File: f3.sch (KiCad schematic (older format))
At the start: 13 parts, among them U7 STM32F303K8Tx, Y1 Crystal

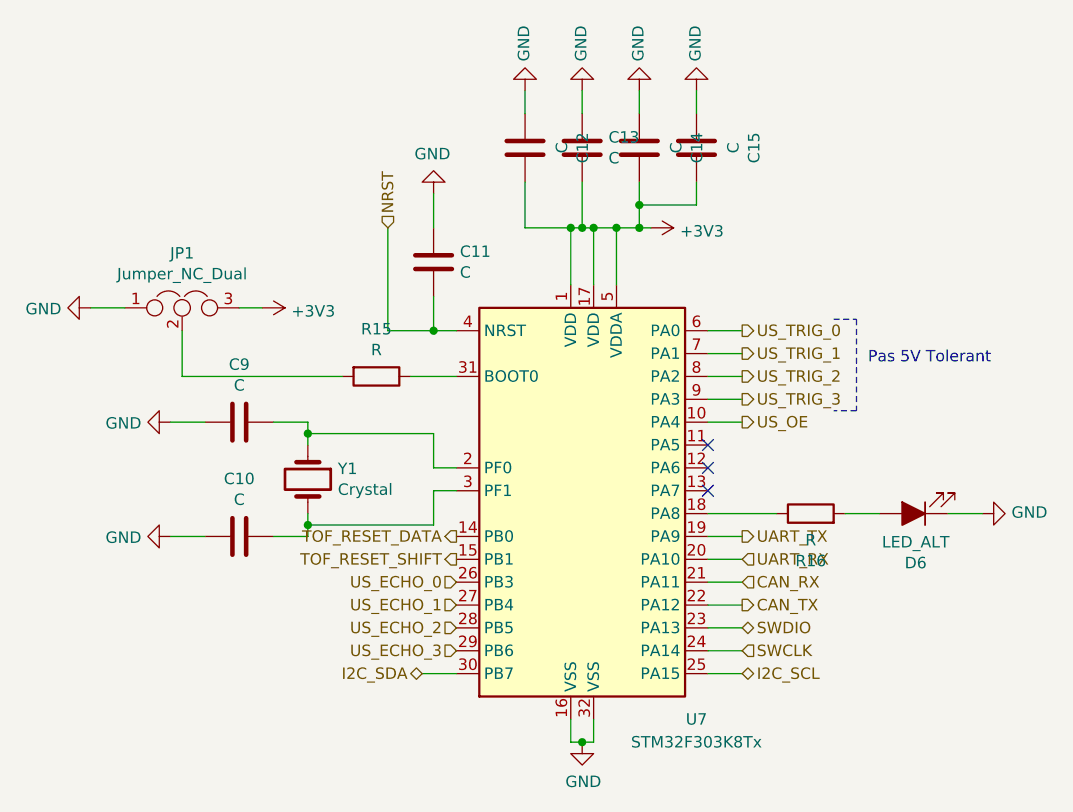
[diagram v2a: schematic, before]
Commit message: Schematic corrections
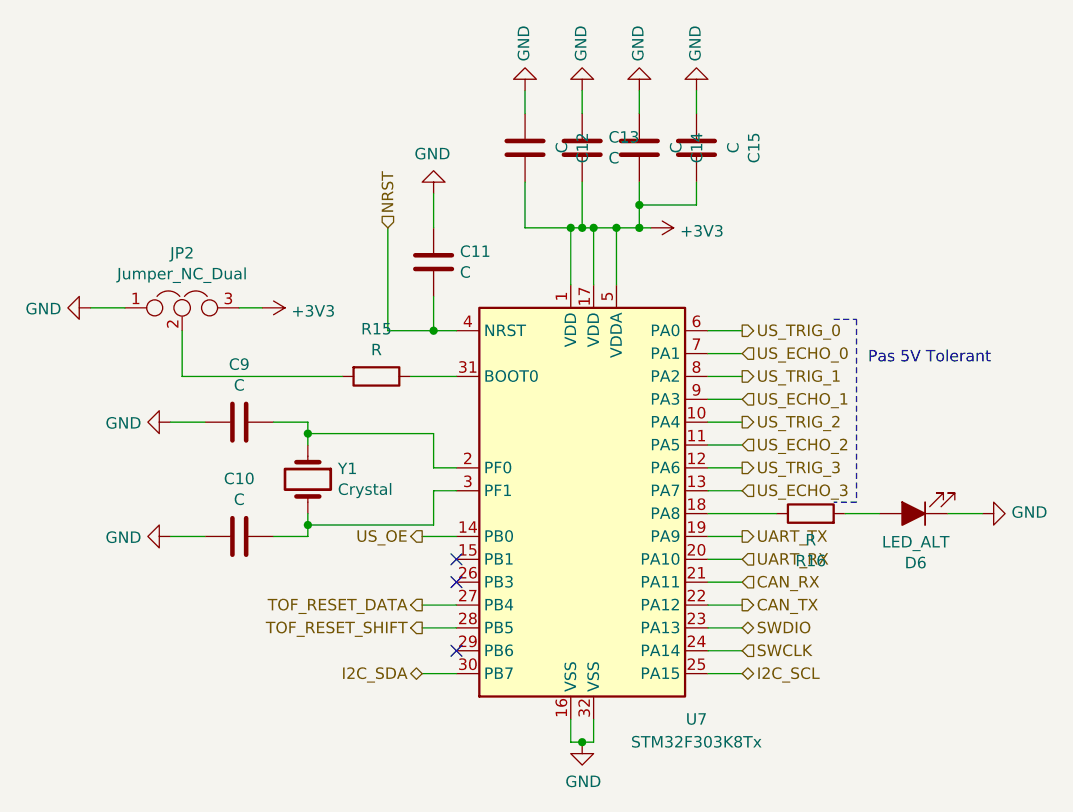
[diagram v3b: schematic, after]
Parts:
- renumbered JP1 to JP2
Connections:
- net TOF_RESET_DATA: now also U7.27 (PB4); no longer U7.14 (PB0)
- net TOF_RESET_SHIFT: now also U7.28 (PB5); no longer U7.15 (PB1)
- net US_ECHO_0: now also U7.7 (PA1); no longer U7.26 (PB3)
- net US_ECHO_1: now also U7.9 (PA3); no longer U7.27 (PB4)
- net US_ECHO_2: now also U7.11 (PA5); no longer U7.28 (PB5)
- net US_ECHO_3: now also U7.13 (PA7); no longer U7.29 (PB6)
- net US_OE: now also U7.14 (PB0); no longer U7.10 (PA4)
- net US_TRIG_1: now also U7.8 (PA2); no longer U7.7 (PA1)
- net US_TRIG_2: now also U7.10 (PA4); no longer U7.8 (PA2)
- net US_TRIG_3: now also U7.12 (PA6); no longer U7.9 (PA3)
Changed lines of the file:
@@
 $EndComp
 $Comp
-L power:GND #PWR059
+L power:GND #PWR058
 U 1 1 5BBD4293
 P 3500 3500
-F 0 "#PWR059" H 3500 3250 50  0001 C CNN
+F 0 "#PWR058" H 3500 3250 50  0001 C CNN
 F 1 "GND" V 3505 3372 50  0000 R CNN
 F 2 "" H 3500 3500 50  0001 C CNN
@@
 $EndComp
 $Comp
-L power:GND #PWR060
+L power:GND #PWR059
 U 1 1 5BBD42C5
 P 3500 4000
-F 0 "#PWR060" H 3500 3750 50  0001 C CNN
+F 0 "#PWR059" H 3500 3750 50  0001 C CNN
 F 1 "GND" V 3505 3872 50  0000 R CNN
 F 2 "" H 3500 4000 50  0001 C CNN
@@
 $EndComp
 $Comp
-L Device:Jumper_NC_Dual JP1
+L Device:Jumper_NC_Dual JP2
 U 1 1 5BBD452E
 P 3550 3000
-F 0 "JP1" H 3550 3239 50  0000 C CNN
+F 0 "JP2" H 3550 3239 50  0000 C CNN
 F 1 "Jumper_NC_Dual" H 3550 3148 50  0000 C CNN
 F 2 "Connector_PinHeader_2.54mm:PinHeader_1x03_P2.54mm_Vertical" H 3550 3000 50  0001 C CNN
@@
 	4550 3300 4750 3300
 $Comp
-L power:GND #PWR058
+L power:GND #PWR057
 U 1 1 5BBD4A9A
 P 3150 3000
-F 0 "#PWR058" H 3150 2750 50  0001 C CNN
+F 0 "#PWR057" H 3150 2750 50  0001 C CNN
 F 1 "GND" V 3155 2872 50  0000 R CNN
 F 2 "" H 3150 3000 50  0001 C CNN
@@
 	3150 3000 3300 3000
 $Comp
-L power:+3V3 #PWR061
+L power:+3V3 #PWR060
 U 1 1 5BBD4C69
 P 3900 3000
-F 0 "#PWR061" H 3900 2850 50  0001 C CNN
+F 0 "#PWR060" H 3900 2850 50  0001 C CNN
 F 1 "+3V3" V 3915 3128 50  0000 L CNN
 F 2 "" H 3900 3000 50  0001 C CNN
@@
 $EndComp
 $Comp
-L power:GND #PWR062
+L power:GND #PWR061
 U 1 1 5BBD55CA
 P 4650 2500
-F 0 "#PWR062" H 4650 2250 50  0001 C CNN
+F 0 "#PWR061" H 4650 2250 50  0001 C CNN
 F 1 "GND" H 4655 2327 50  0000 C CNN
 F 2 "" H 4650 2500 50  0001 C CNN
@@
 	5350 2650 5450 2650
 $Comp
-L power:+3V3 #PWR067
+L power:+3V3 #PWR066
 U 1 1 5BBD6204
 P 5600 2650
-F 0 "#PWR067" H 5600 2500 50  0001 C CNN
+F 0 "#PWR066" H 5600 2500 50  0001 C CNN
 F 1 "+3V3" V 5615 2778 50  0000 L CNN
 F 2 "" H 5600 2650 50  0001 C CNN
@@
 $EndComp
 $Comp
-L power:GND #PWR068
+L power:GND #PWR067
 U 1 1 5BBD68AE
 P 5800 2050
-F 0 "#PWR068" H 5800 1800 50  0001 C CNN
+F 0 "#PWR067" H 5800 1800 50  0001 C CNN
 F 1 "GND" V 5805 1922 50  0000 R CNN
 F 2 "" H 5800 2050 50  0001 C CNN
@@
 $EndComp
 $Comp
-L power:GND #PWR066
+L power:GND #PWR065
 U 1 1 5BBD68FC
 P 5550 2050
-F 0 "#PWR066" H 5550 1800 50  0001 C CNN
+F 0 "#PWR065" H 5550 1800 50  0001 C CNN
 F 1 "GND" V 5555 1922 50  0000 R CNN
 F 2 "" H 5550 2050 50  0001 C CNN
@@
 $EndComp
 $Comp
-L power:GND #PWR064
+L power:GND #PWR063
 U 1 1 5BBD694A
 P 5300 2050
-F 0 "#PWR064" H 5300 1800 50  0001 C CNN
+F 0 "#PWR063" H 5300 1800 50  0001 C CNN
 F 1 "GND" V 5305 1922 50  0000 R CNN
 F 2 "" H 5300 2050 50  0001 C CNN
@@
 $EndComp
 $Comp
-L power:GND #PWR063
+L power:GND #PWR062
 U 1 1 5BBD6998
 P 5050 2050
-F 0 "#PWR063" H 5050 1800 50  0001 C CNN
+F 0 "#PWR062" H 5050 1800 50  0001 C CNN
 F 1 "GND" V 5055 1922 50  0000 R CNN
 F 2 "" H 5050 2050 50  0001 C CNN
@@
 	5550 2550 5550 2650
 $Comp
-L power:GND #PWR065
+L power:GND #PWR064
 U 1 1 5BBDA4B0
 P 5300 4900
-F 0 "#PWR065" H 5300 4650 50  0001 C CNN
+F 0 "#PWR064" H 5300 4650 50  0001 C CNN
 F 1 "GND" H 5305 4727 50  0000 C CNN
 F 2 "" H 5300 4900 50  0001 C CNN
@@
 $EndComp
 $Comp
-L power:GND #PWR069
+L power:GND #PWR068
 U 1 1 5BBDC410
 P 7050 3900
-F 0 "#PWR069" H 7050 3650 50  0001 C CNN
+F 0 "#PWR068" H 7050 3650 50  0001 C CNN
 F 1 "GND" V 7055 3772 50  0000 R CNN
 F 2 "" H 7050 3900 50  0001 C CNN
@@
 Text HLabel 6000 3100 2    50   Output ~ 0
 US_TRIG_0
-Text HLabel 6000 3200 2    50   Output ~ 0
+Text HLabel 6000 3300 2    50   Output ~ 0
 US_TRIG_1
-Text HLabel 6000 3300 2    50   Output ~ 0
+Text HLabel 6000 3500 2    50   Output ~ 0
 US_TRIG_2
-Text HLabel 6000 3400 2    50   Output ~ 0
+Text HLabel 6000 3700 2    50   Output ~ 0
 US_TRIG_3
-Text HLabel 4750 4200 0    50   Input ~ 0
+Text HLabel 6000 3200 2    50   Input ~ 0
 US_ECHO_0
-Text HLabel 4750 4300 0    50   Input ~ 0
+Text HLabel 6000 3400 2    50   Input ~ 0
 US_ECHO_1
-Text HLabel 4750 4400 0    50   Input ~ 0
+Text HLabel 6000 3600 2    50   Input ~ 0
 US_ECHO_2
-Text HLabel 4750 4500 0    50   Input ~ 0
-US_ECHO_3
-Text HLabel 4750 4000 0    50   Output ~ 0
+Text HLabel 4600 4300 0    50   Output ~ 0
 TOF_RESET_DATA
-Text HLabel 4750 4100 0    50   Output ~ 0
+Text HLabel 4600 4400 0    50   Output ~ 0
 TOF_RESET_SHIFT
-NoConn ~ 5850 3800
-NoConn ~ 5850 3700
-NoConn ~ 5850 3600
 Text Notes 6550 3250 0    50   ~ 0
 Pas 5V Tolerant
 Wire Notes Line
 	6400 3050 6500 3050
-Wire Notes Line
-	6500 3050 6500 3450
-Wire Notes Line
-	6500 3450 6400 3450
-Text HLabel 6000 3500 2    50   Output ~ 0
+Text HLabel 4600 4000 0    50   Output ~ 0
 US_OE
 Wire Wire Line
@@
 	0    1    1    0
 $EndComp
+Wire Wire Line
+	5850 3600 6000 3600
+Wire Wire Line
+	5850 3700 6000 3700
+Text HLabel 6000 3800 2    50   Input ~ 0
+US_ECHO_3
+Wire Notes Line
+	6500 3850 6400 3850
+Wire Notes Line
+	6500 3050 6500 3850
+Wire Wire Line
+	5850 3800 6000 3800
+Wire Wire Line
+	4600 4000 4750 4000
+Wire Wire Line
+	4600 4300 4750 4300
+Wire Wire Line
+	4600 4400 4750 4400
+NoConn ~ 4750 4200
+NoConn ~ 4750 4500
+NoConn ~ 4750 4100
 $EndSCHEMATC

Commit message: Corrected, routing redone
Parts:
- JP2: footprint Connector_PinHeader_2.54mm:PinHeader_1x03_P2.54mm_Vertical -> Jumper:SolderJumper-3_P1.3mm_Open_RoundedPad1.0x1.5mm
- Y1: footprint Crystal:Crystal_HC49-U_Vertical -> Crystal:Crystal_HC49-4H_Vertical
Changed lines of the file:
@@
 F 0 "JP2" H 3550 3239 50  0000 C CNN
 F 1 "Jumper_NC_Dual" H 3550 3148 50  0000 C CNN
-F 2 "Connector_PinHeader_2.54mm:PinHeader_1x03_P2.54mm_Vertical" H 3550 3000 50  0001 C CNN
+F 2 "Jumper:SolderJumper-3_P1.3mm_Open_RoundedPad1.0x1.5mm" H 3550 3000 50  0001 C CNN
 F 3 "~" H 3550 3000 50  0001 C CNN
 	1    3550 3000
@@
 F 0 "Y1" V 4054 3881 50  0000 L CNN
 F 1 "Crystal" V 4145 3881 50  0000 L CNN
-F 2 "Crystal:Crystal_HC49-U_Vertical" H 4100 3750 50  0001 C CNN
+F 2 "Crystal:Crystal_HC49-4H_Vertical" H 4100 3750 50  0001 C CNN
 F 3 "~" H 4100 3750 50  0001 C CNN
 	1    4100 3750

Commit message: Added RS refs
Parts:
- D6: RS (none) -> 174-9844,174-9849
- Y1: RS (none) -> 814-9440
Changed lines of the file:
@@
 F 2 "LED_SMD:LED_0805_2012Metric_Castellated" H 6750 3900 50  0001 C CNN
 F 3 "~" H 6750 3900 50  0001 C CNN
+F 4 "174-9844,174-9849" H 0   0   50  0001 C CNN "RS"
 	1    6750 3900
 	-1   0    0    1
@@
 F 2 "Crystal:Crystal_HC49-4H_Vertical" H 4100 3750 50  0001 C CNN
 F 3 "~" H 4100 3750 50  0001 C CNN
+F 4 "814-9440" H 0   0   50  0001 C CNN "RS"
 	1    4100 3750
 	0    1    1    0

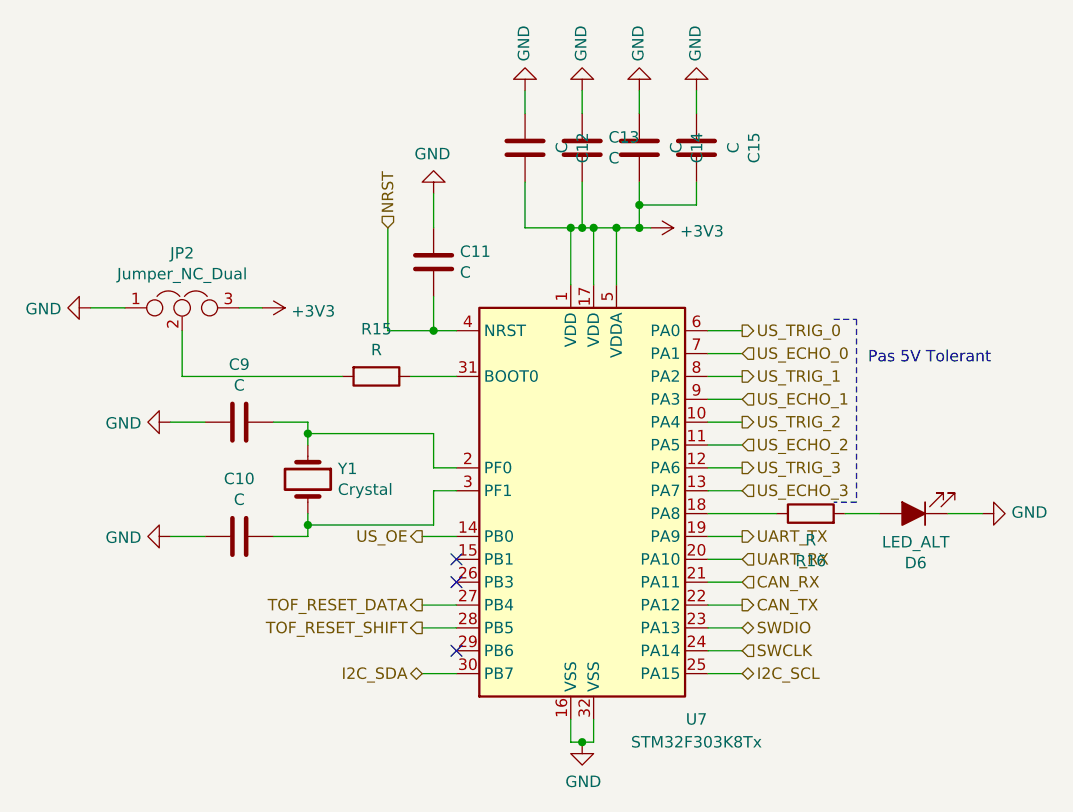
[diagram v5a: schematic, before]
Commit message: Added component values
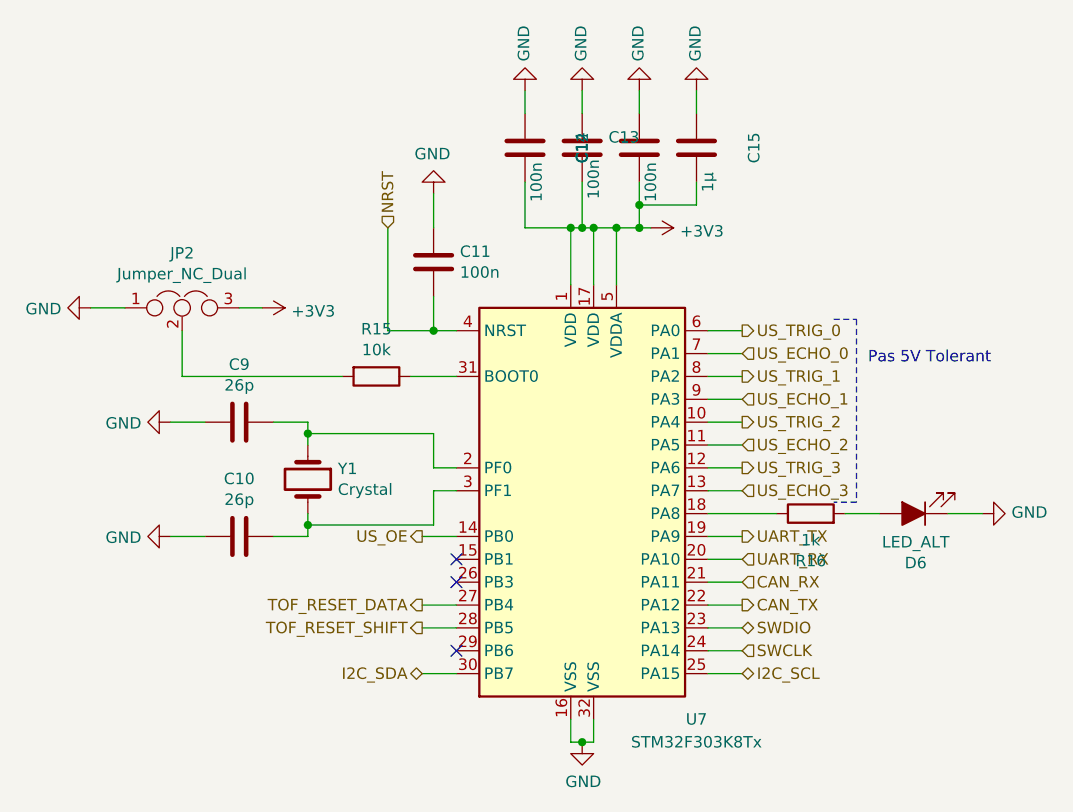
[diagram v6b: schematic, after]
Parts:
- C10, C9: value C -> 26p
- C11, C12, C13, C14: value C -> 100n
- C15: value C -> 1µ
- R15: value R -> 10k
- R16: value R -> 1k
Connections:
- net +3V3: now also C14.2; no longer C14.1
- net GND: now also C14.1; no longer C14.2
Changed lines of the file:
@@
 EESchema Schematic File Version 4
-LIBS:ultraphotonicsense-elec-cache
 EELAYER 26 0
 EELAYER END
@@
 P 3800 3500
 F 0 "C9" V 3548 3500 50  0000 C CNN
-F 1 "C" V 3639 3500 50  0000 C CNN
+F 1 "26p" V 3639 3500 50  0000 C CNN
 F 2 "Capacitor_SMD:C_0805_2012Metric_Pad1.15x1.40mm_HandSolder" H 3838 3350 50  0001 C CNN
 F 3 "~" H 3800 3500 50  0001 C CNN
@@
 P 3800 4000
 F 0 "C10" V 3548 4000 50  0000 C CNN
-F 1 "C" V 3639 4000 50  0000 C CNN
+F 1 "26p" V 3639 4000 50  0000 C CNN
 F 2 "Capacitor_SMD:C_0805_2012Metric_Pad1.15x1.40mm_HandSolder" H 3838 3850 50  0001 C CNN
 F 3 "~" H 3800 4000 50  0001 C CNN
@@
 P 4400 3300
 F 0 "R15" V 4193 3300 50  0000 C CNN
-F 1 "R" V 4284 3300 50  0000 C CNN
+F 1 "10k" V 4284 3300 50  0000 C CNN
 F 2 "Resistor_SMD:R_0805_2012Metric_Pad1.15x1.40mm_HandSolder" V 4330 3300 50  0001 C CNN
 F 3 "~" H 4400 3300 50  0001 C CNN
@@
 P 4650 2800
 F 0 "C11" H 4765 2846 50  0000 L CNN
-F 1 "C" H 4765 2755 50  0000 L CNN
+F 1 "100n" H 4765 2755 50  0000 L CNN
 F 2 "Capacitor_SMD:C_0805_2012Metric_Pad1.15x1.40mm_HandSolder" H 4688 2650 50  0001 C CNN
 F 3 "~" H 4650 2800 50  0001 C CNN
@@
 P 5050 2300
 F 0 "C12" V 4798 2300 50  0000 C CNN
-F 1 "C" V 4889 2300 50  0000 C CNN
+F 1 "100n" V 5000 2450 50  0000 C CNN
 F 2 "Capacitor_SMD:C_0805_2012Metric_Pad1.15x1.40mm_HandSolder" H 5088 2150 50  0001 C CNN
 F 3 "~" H 5050 2300 50  0001 C CNN
@@
 P 5300 2300
 F 0 "C13" H 5185 2346 50  0000 R CNN
-F 1 "C" H 5185 2255 50  0000 R CNN
+F 1 "100n" V 5250 2250 50  0000 R CNN
 F 2 "Capacitor_SMD:C_0805_2012Metric_Pad1.15x1.40mm_HandSolder" H 5338 2150 50  0001 C CNN
 F 3 "~" H 5300 2300 50  0001 C CNN
@@
 P 5550 2300
 F 0 "C14" V 5298 2300 50  0000 C CNN
-F 1 "C" V 5389 2300 50  0000 C CNN
+F 1 "100n" V 5600 2150 50  0000 C CNN
 F 2 "Capacitor_SMD:C_0805_2012Metric_Pad1.15x1.40mm_HandSolder" H 5588 2150 50  0001 C CNN
 F 3 "~" H 5550 2300 50  0001 C CNN
 	1    5550 2300
-	-1   0    0    1
+	1    0    0    -1
 $EndComp
 $Comp
@@
 P 5800 2300
 F 0 "C15" V 5548 2300 50  0000 C CNN
-F 1 "C" V 5639 2300 50  0000 C CNN
+F 1 "1µ" V 5750 2450 50  0000 C CNN
 F 2 "Capacitor_SMD:C_0805_2012Metric_Pad1.15x1.40mm_HandSolder" H 5838 2150 50  0001 C CNN
 F 3 "~" H 5800 2300 50  0001 C CNN
@@
 P 6300 3900
 F 0 "R16" V 6093 3900 50  0000 C CNN
-F 1 "R" V 6184 3900 50  0000 C CNN
+F 1 "1k" V 6184 3900 50  0000 C CNN
 F 2 "Resistor_SMD:R_0805_2012Metric_Pad1.15x1.40mm_HandSolder" V 6230 3900 50  0001 C CNN
 F 3 "~" H 6300 3900 50  0001 C CNN

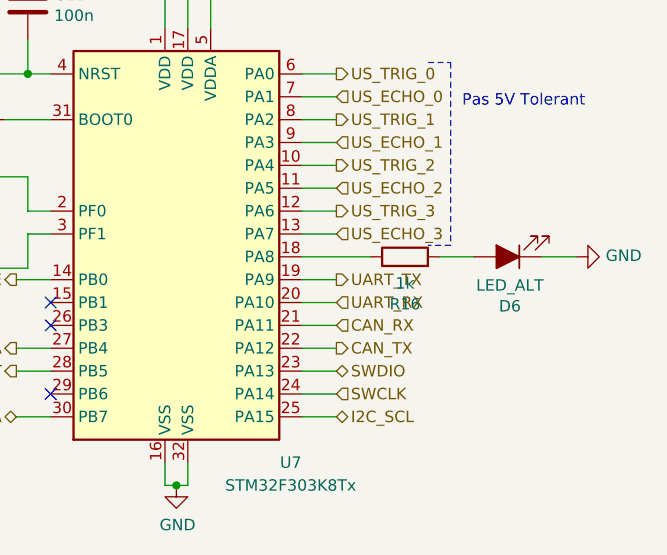
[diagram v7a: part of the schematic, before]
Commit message: Added resistors values
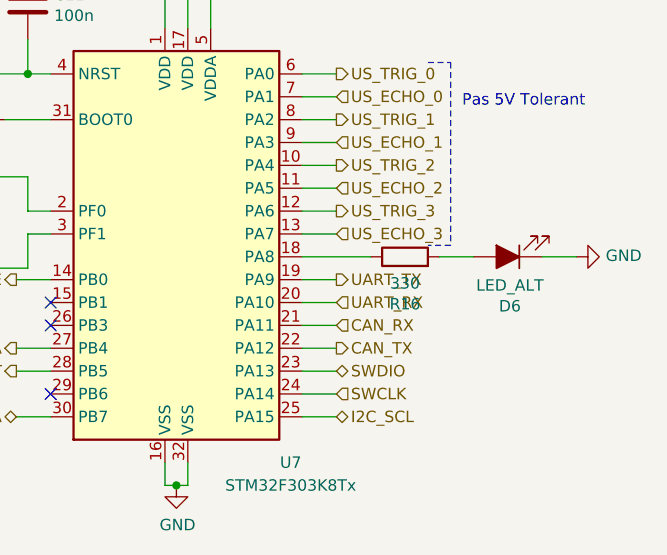
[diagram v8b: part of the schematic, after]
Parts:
- R16: value 1k -> 330
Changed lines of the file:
@@
 P 6300 3900
 F 0 "R16" V 6093 3900 50  0000 C CNN
-F 1 "1k" V 6184 3900 50  0000 C CNN
+F 1 "330" V 6184 3900 50  0000 C CNN
 F 2 "Resistor_SMD:R_0805_2012Metric_Pad1.15x1.40mm_HandSolder" V 6230 3900 50  0001 C CNN
 F 3 "~" H 6300 3900 50  0001 C CNN
